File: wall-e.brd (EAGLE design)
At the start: 62.2 x 51.9 mm, 71 parts, among them IC1 VREG-TS1117CW-3V3, T1 BC847, U1 TSM2306CX, U2 TSM2306CX, U3 TSM2306CX, U4 TSM2306CX, U5 TSM2306CX, U6 TSM2306CX, U7 TSM2306CX, U8 LM293AD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

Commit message: WIP small board fixes and BOM
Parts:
- moved C10 2.09 mm to (74.4, 23.7), turned to 180 degrees
- moved C9 2.00 mm to (67.1, 23.7)
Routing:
- net +5V: track 241.8 -> 225.6 mm, vias 15 -> 14
- net +12V: track 161.8 -> 164.1 mm, vias 4 -> 2
- net GND: track 136.0 -> 134.5 mm, vias 125 -> 95
- net N$19: track 31.4 -> 32.8 mm
- net CODEUSE1: track 121.4 -> 120.8 mm

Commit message: fixed board
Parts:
- C14: value 10nF -> 100nF
- C3: value 1uF -> 4.7uF
- C9: device resistor:E2,5-7 -> resistor:E3,5-8
- moved LED1 4.37 mm to (75.7, 44.9), turned to 270 degrees
- moved C10 1.44 mm to (75.8, 23.4), turned to 270 degrees
- moved C9 1.06 mm to (67.9, 23.0)
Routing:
- net GND: track 134.5 -> 127.0 mm, vias 95 -> 92
- net N$18: track 3.57 -> 9.57 mm
- net +5V: track 225.6 -> 228.1 mm
- net SENSOR4: track 24.5 -> 23.6 mm
- net N$5: track 17.6 -> 18.3 mm
- net +12V: track 164.1 -> 164.6 mm
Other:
- board text added: "TelecomRobotics"
- board text removed: "Telecom Robotics"

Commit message: Minor changes
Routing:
- net GND: track 127.0 -> 123.4 mm
- net N$23: track 47.9 -> 46.8 mm
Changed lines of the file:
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@@
 <wire x1="65.94" y1="35.11" x2="65.83" y2="35.21" width="0.4064" layer="16"/>
 <wire x1="65.83" y1="35.21" x2="65.83" y2="36.21" width="0.4064" layer="16"/>
-<wire x1="65.83" y1="36.21" x2="69.39" y2="35.81" width="0.4064" layer="1"/>
 <via x="75.45" y="36.94" extent="1-16" drill="0.5"/>
 <wire x1="78.05" y1="48.78" x2="79.46" y2="48.78" width="0.254" layer="1"/>
-<wire x1="80.03" y1="48.21" x2="79.46" y2="48.78" width="0.4064" layer="1"/>
+<wire x1="80.03" y1="48.21" x2="79.46" y2="48.78" width="0.254" layer="1"/>
 <via x="80.03" y="48.21" extent="1-16" drill="0.5"/>
 <wire x1="78.05" y1="47.28" x2="79.1" y2="47.28" width="0.254" layer="1"/>
-<wire x1="79.1" y1="47.28" x2="80.03" y2="48.21" width="0.4064" layer="1"/>
+<wire x1="79.1" y1="47.28" x2="80.03" y2="48.21" width="0.254" layer="1"/>
 <wire x1="83.3" y1="45.03" x2="83.3" y2="45.83" width="0.254" layer="1"/>
 <wire x1="83.3" y1="45.83" x2="82.21" y2="46.92" width="0.254" layer="1"/>
@@
 <wire x1="85.15" y1="51.12" x2="86.36" y2="51.12" width="0.254" layer="16"/>
 <wire x1="80.3" y1="54.03" x2="80.3" y2="50.27" width="0.254" layer="1"/>
-<wire x1="80.3" y1="50.27" x2="80.72" y2="50.27" width="0.4064" layer="1"/>
+<wire x1="80.3" y1="50.27" x2="80.72" y2="50.27" width="0.254" layer="1"/>
 <via x="110.22" y="45.38" extent="1-16" drill="0.5"/>
 <wire x1="111.96" y1="48.77" x2="111.96" y2="45.38" width="0.4064" layer="1"/>
@@
 <contactref element="JP2" pad="7"/>
 <contactref element="JP2" pad="4"/>
-<wire x1="87.5" y1="53.1" x2="87.5" y2="53.3" width="0.4064" layer="1"/>
 <via x="87.5" y="53.1" extent="1-16" drill="0.5"/>
 <wire x1="87.5" y1="53.02" x2="86.36" y2="53.02" width="0.4064" layer="16"/>
@@
 <wire x1="87.5" y1="53.1" x2="88.54" y2="53.1" width="0.4064" layer="16"/>
 <wire x1="88.54" y1="53.1" x2="88.54" y2="53.03" width="0.4064" layer="16"/>
-<wire x1="79.8" y1="54.03" x2="79.8" y2="54.8" width="0.254" layer="1"/>
-<wire x1="79.8" y1="54.8" x2="79.1" y2="54.8" width="0.254" layer="1"/>
-<via x="79.1" y="54.8" extent="1-16" drill="0.5"/>
-<wire x1="79.02" y1="54.8" x2="79.1" y2="54.8" width="0.4064" layer="16"/>
+<via x="79" y="55" extent="1-16" drill="0.5"/>
+<wire x1="79.02" y1="54.8" x2="79" y2="55" width="0.4064" layer="16"/>
 <wire x1="79.02" y1="54.8" x2="79.02" y2="53.73" width="0.4064" layer="16"/>
 <wire x1="83.8" y1="45.03" x2="83.8" y2="47.14" width="0.254" layer="1"/>
@@
 <wire x1="79.82" y1="64.08" x2="79.84" y2="57.58" width="0.4064" layer="1"/>
 <via x="79.84" y="57.58" extent="1-16" drill="0.5"/>
-<wire x1="79.1" y1="56.84" x2="79.84" y2="57.58" width="0.4064" layer="16"/>
-<wire x1="79.1" y1="54.8" x2="79.1" y2="56.84" width="0.4064" layer="16"/>
 <wire x1="84.47" y1="45.18" x2="84.86" y2="44.79" width="0.4064" layer="16"/>
 <wire x1="84.86" y1="44.79" x2="84.86" y2="44.64" width="0.4064" layer="16"/>
@@
 <wire x1="84.64" y1="51.3" x2="86.36" y2="53.02" width="0.4064" layer="16"/>
 <wire x1="84.64" y1="49.87" x2="84.64" y2="51.3" width="0.4064" layer="16"/>
-<wire x1="79.1" y1="54.8" x2="79.21" y2="54.8" width="0.4064" layer="16"/>
 <wire x1="86.92" y1="40.48" x2="85.67" y2="40.48" width="0.4064" layer="1"/>
 <wire x1="86.92" y1="40.48" x2="86.92" y2="40.45" width="0.4064" layer="1"/>
@@
 <wire x1="101.37" y1="24.44" x2="97.24" y2="24.44" width="0.4064" layer="1"/>
 <wire x1="86.36" y1="53.02" x2="86.36" y2="55.22" width="0.4064" layer="16"/>
-<wire x1="84.74" y1="56.84" x2="79.1" y2="56.84" width="0.4064" layer="16"/>
+<wire x1="84.74" y1="56.84" x2="79.84" y2="56.84" width="0.4064" layer="16"/>
 <wire x1="86.36" y1="55.22" x2="84.74" y2="56.84" width="0.4064" layer="16"/>
 <wire x1="84.47" y1="46.7" x2="83.8" y2="46.7" width="0.4064" layer="16"/>
@@
 <wire x1="90.08" y1="26.54" x2="90.88" y2="26.54" width="0.4064" layer="1"/>
 <wire x1="90.88" y1="26.54" x2="90.9" y2="26.52" width="0.4064" layer="1"/>
+<wire x1="79" y1="55" x2="79.8" y2="55" width="0.254" layer="1"/>
+<wire x1="79.8" y1="55" x2="79.8" y2="54.03" width="0.254" layer="1"/>
+<wire x1="79" y1="55" x2="79.1" y2="55" width="0.4064" layer="16"/>
+<wire x1="79.1" y1="55" x2="79.1" y2="56.84" width="0.4064" layer="16"/>
+<wire x1="79.1" y1="56.84" x2="79.84" y2="56.84" width="0.4064" layer="16"/>
+<wire x1="79.84" y1="56.84" x2="79.84" y2="57.58" width="0.4064" layer="16"/>
 </signal>
 <signal name="VALVE1">
@@
 <via x="97.07" y="45.28" extent="1-16" drill="0.5"/>
 <via x="93.64" y="38.14" extent="1-16" drill="0.5"/>
-<wire x1="94.51" y1="26.37" x2="93.87" y2="25.73" width="0.4064" layer="1"/>
 <wire x1="100.06" y1="49.09" x2="100.33" y2="49.36" width="0.254" layer="16"/>
 <wire x1="100.33" y1="49.36" x2="105.29" y2="49.36" width="0.254" layer="16"/>
@@
 <wire x1="111.22" y1="44.58" x2="111.22" y2="42.76" width="0.254" layer="1"/>
 <wire x1="111.22" y1="42.76" x2="111.23" y2="42.76" width="0.4064" layer="1"/>
-<wire x1="92.34" y1="38.61" x2="92.11" y2="38.61" width="0.4064" layer="1"/>
 <wire x1="93.87" y1="25.73" x2="93.77" y2="25.83" width="0.254" layer="1"/>
 <wire x1="93.77" y1="38.01" x2="93.77" y2="25.83" width="0.254" layer="1"/>

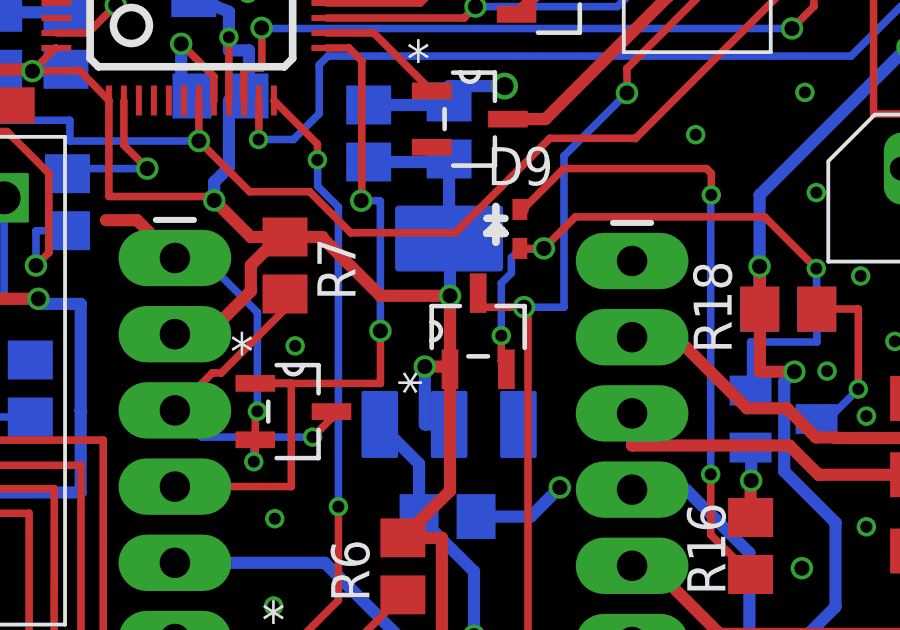
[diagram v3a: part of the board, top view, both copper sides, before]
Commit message: Correction of a defect found by eurocircuit (useless trace)
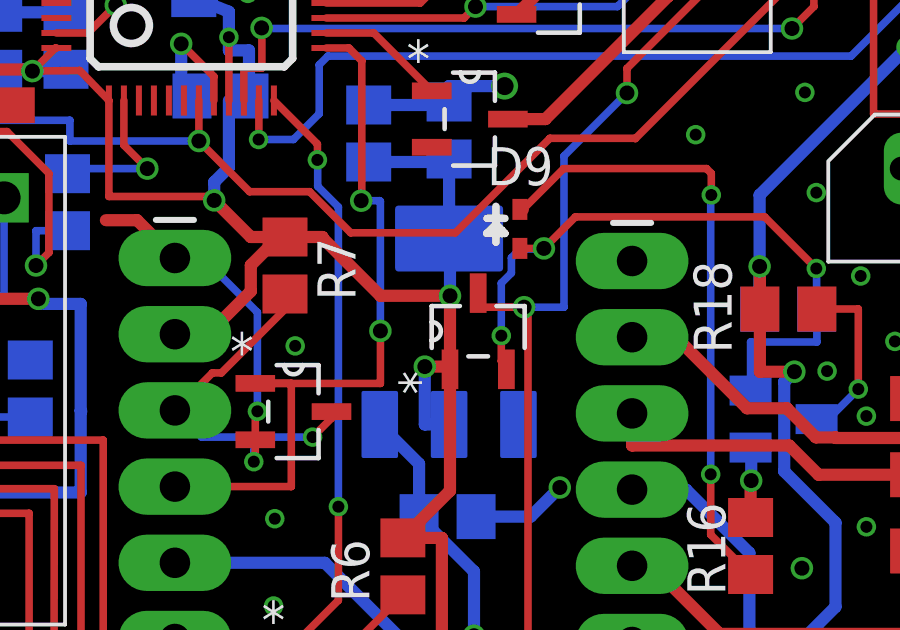
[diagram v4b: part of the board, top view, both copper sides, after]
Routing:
- net +3V3: track 187.1 -> 185.8 mm
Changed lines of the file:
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@@
 <wire x1="91.14" y1="40.429" x2="91.1702" y2="40.429" width="0.4064" layer="16"/>
 <wire x1="91.1702" y1="38.52" x2="91.1702" y2="40.429" width="0.4064" layer="16"/>
-<wire x1="91.1702" y1="37.24" x2="91.1702" y2="38.52" width="0.4064" layer="16"/>
 <wire x1="78.83" y1="46.03" x2="79.8" y2="45.03" width="0.254" layer="1"/>
 <wire x1="77.25" y1="46.01" x2="78.83" y2="46.03" width="0.254" layer="1"/>
